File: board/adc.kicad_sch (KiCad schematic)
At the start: 8 parts, among them U1 MCP3428

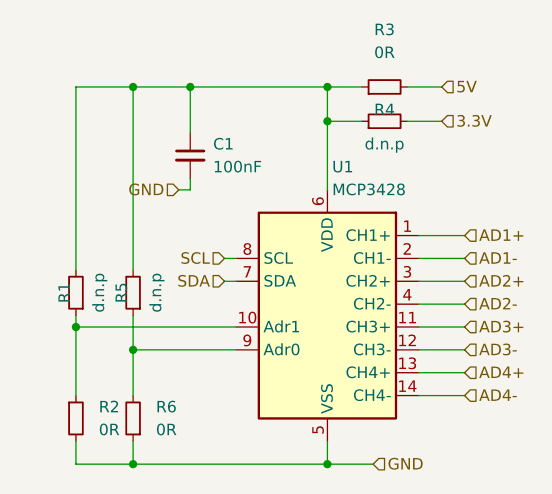
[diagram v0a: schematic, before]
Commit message: added copper pours and moved edgy specific components out of the subsheet
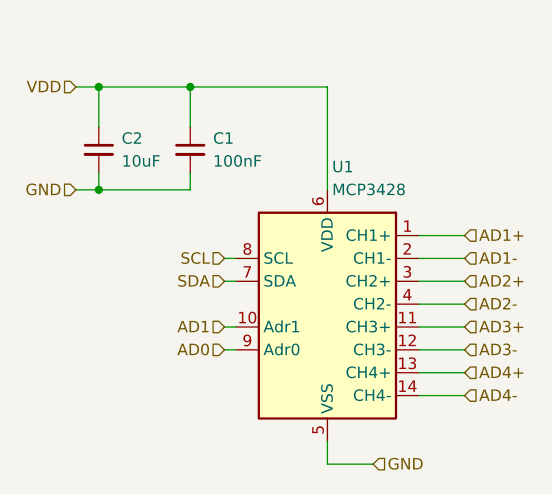
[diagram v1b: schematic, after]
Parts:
- removed R1, R4, R5: d.n.p, Resistor_SMD:R_0603_1608Metric, symbol Device:R_Small
- removed R2, R3, R6: 0R, Resistor_SMD:R_0603_1608Metric, symbol Device:R_Small
- added C2: 10uF, Capacitor_SMD:C_0603_1608Metric, symbol Device:C_Small
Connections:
- net GND: now also C2.2
- net AD1: now reaches U1.10 (Adr1)
- net VDD: now reaches C1.1, U1.6 (VDD)
- net VDD: now also C2.1
- net AD0: now reaches U1.9 (Adr0)
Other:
- moved on the sheet: C1
